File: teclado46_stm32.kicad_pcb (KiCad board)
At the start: 2 copper layers, 232.6 x 80.6 mm, 159 parts, among them J1 78171-0004, U1 XC6206PxxxMR, U2 STM32G0B1CBTx

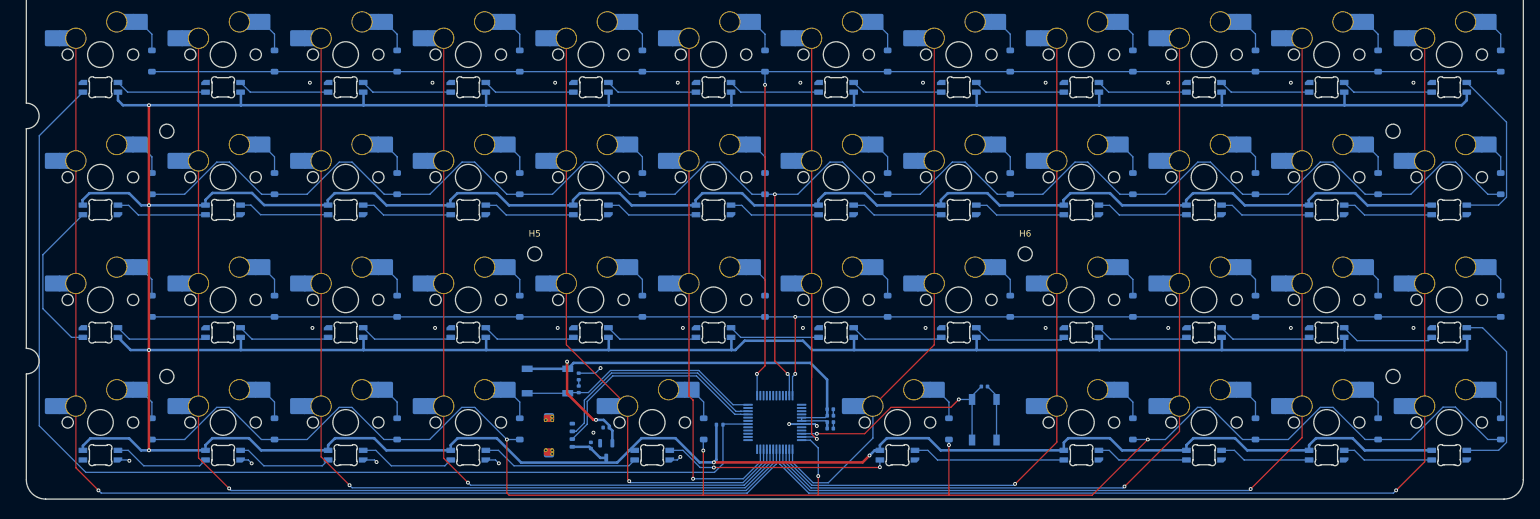
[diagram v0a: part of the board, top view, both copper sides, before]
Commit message: chore: rerouted rows
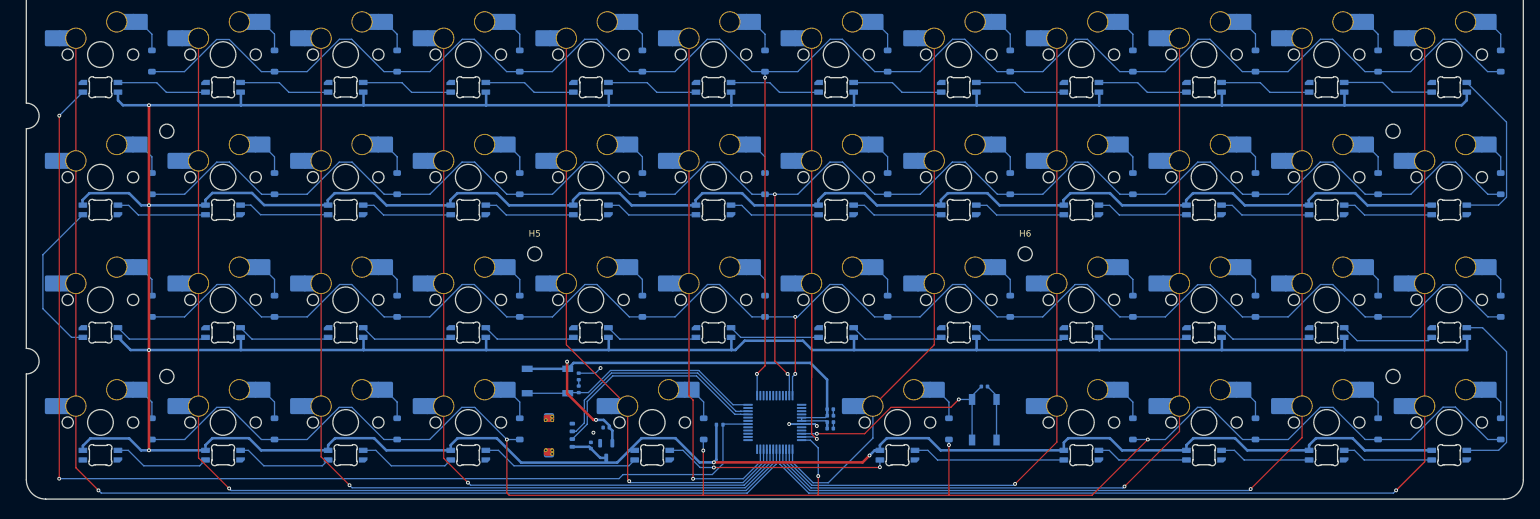
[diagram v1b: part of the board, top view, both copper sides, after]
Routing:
- net ROW 0: track 260.4 -> 306.2 mm
- net ROW 2: track 222.0 -> 267.8 mm
- net GND: track 28.4 -> 18.4 mm, vias 29 -> 4
- net RGB3V: track 174.3 -> 175.5 mm, vias 0 -> 2

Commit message: chore: neater routing
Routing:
- net +5V: track 993.5 -> 992.8 mm
- net Net-(LED39-DIN): track 15.0 -> 14.2 mm
- net Net-(LED38-DIN): track 15.0 -> 14.2 mm
- net Net-(LED37-DIN): track 15.0 -> 14.2 mm

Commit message: chore: add decoupling caps for 5v led lines
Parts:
- added C10: 100n, Capacitor_SMD:C_0402_1005Metric, B.Cu at (41.3, 58.8)
- added C11: 100n, Capacitor_SMD:C_0402_1005Metric, B.Cu at (43.7, 46.5)
- added C8: 100n, Capacitor_SMD:C_0402_1005Metric, B.Cu at (113.1, 100.8)
- added C9: 100n, Capacitor_SMD:C_0402_1005Metric, B.Cu at (44.1, 84.5)
